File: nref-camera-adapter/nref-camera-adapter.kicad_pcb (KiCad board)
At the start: 4 copper layers, 52.2 x 11.9 mm, 4 parts, among them J1 Conn_01x20, J2 Conn_01x24

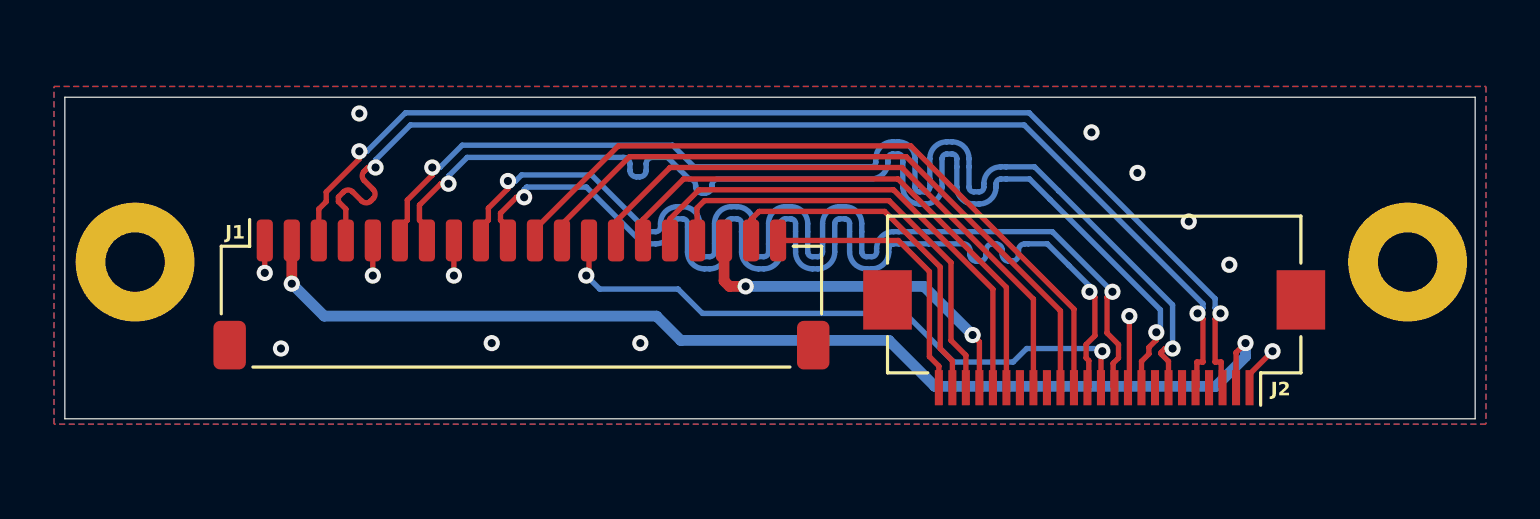
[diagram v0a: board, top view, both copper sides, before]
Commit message: camera-adapter: mech. and routing update
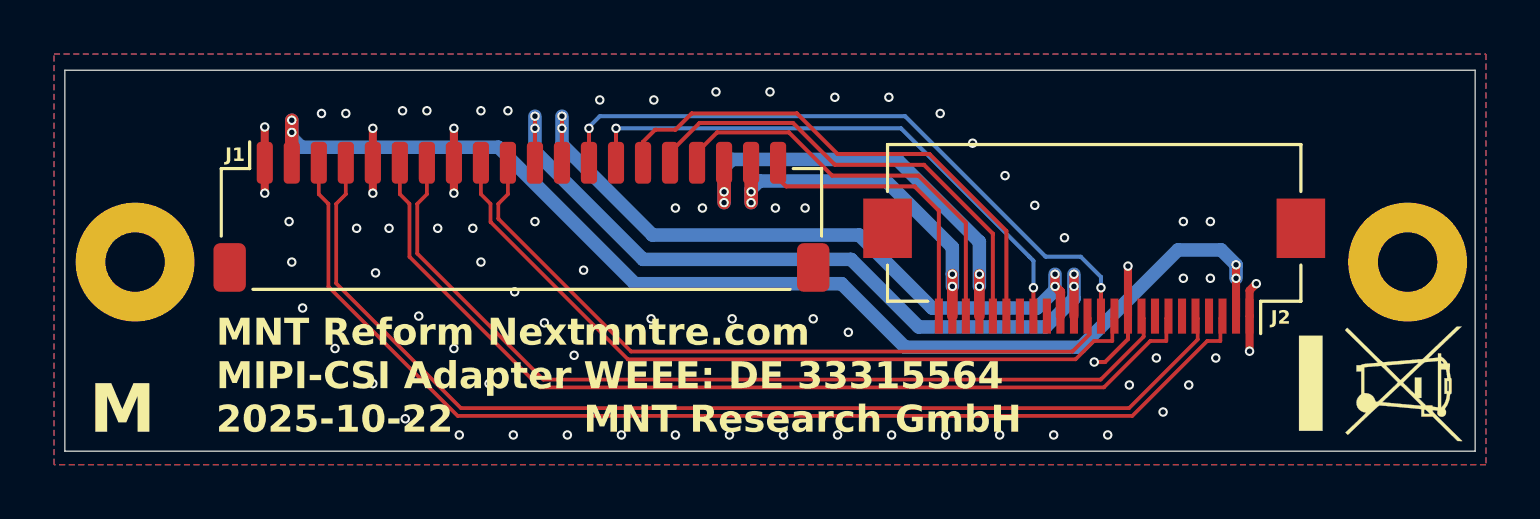
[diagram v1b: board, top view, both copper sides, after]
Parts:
- added REF**: WEEE-Logo_4.2x6mm_SilkScreen, Symbol:WEEE-Logo_4.2x6mm_SilkScreen, F.Cu at (163.1, 100.0)
- moved J1 2.88 mm to (131.3, 93.8)
- moved J2 2.65 mm to (152.5, 95.7)
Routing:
- net /CAM_MIPI_D1P: track 42.1 -> 27.1 mm, vias 2 -> 0
- net /CAM_MIPI_D1N: track 42.2 -> 28.7 mm, vias 2 -> 0
- net /CAM_MIPI_CP: track 42.4 -> 33.8 mm, vias 2 -> 0
- net /CAM_MIPI_CN: track 42.4 -> 35.3 mm, vias 2 -> 0
- net GND: track 8.17 -> 14.2 mm, vias 13 -> 77
- net /CAM_AF_VCC: track 41.2 -> 44.5 mm, vias 2 -> 4
- net /CAM_AVDD: track 13.6 -> 16.8 mm, vias 2 -> 4
- net /CAM_MIPI_D0P: track 42.7 -> 40.4 mm, vias 2 -> 0
- net /CAM_DVDD: track 25.3 -> 27.3 mm, vias 0 -> 4
- net /CAM_DOVDD: track 27.1 -> 28.6 mm, vias 0 -> 4
- net /CAM_PWDNB: track 22.3 -> 20.8 mm, vias 0 -> 2
- net /CAM_SDA: track 16.5 -> 15.5 mm
- net /CAM_MCLK: track 23.4 -> 24.4 mm
- net /CAM_MIPI_D0N: track 42.7 -> 41.8 mm, vias 2 -> 0
- net /CAM_SCL: track 18.4 -> 17.5 mm
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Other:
- board size 52.2 x 11.9 mm -> 52.2 x 14.1 mm
- board text added: "0.8mm PCB, 4 layers stackup: JLC04081H-3313 90ohm diff impedance trace width: 0.xx mm spacing: 0.x mm"
- board text added: "M"
- board text added: "MNT Reform Next MIPI-CSI Adapter 2025-10-22"
- board text added: "mntre.com WEEE: DE 33315564 MNT Research GmbH"
